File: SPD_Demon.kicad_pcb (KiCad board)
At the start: 2 copper layers, 146 x 21.1 mm, 3 parts, among them J1 Conn_02x84_Top_Bottom, U1 AT24CS02-SSHM, U2 AT24CS02-SSHM

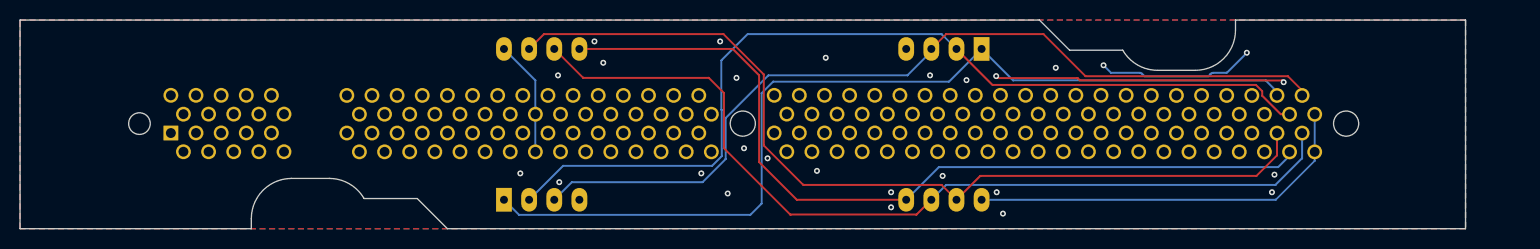
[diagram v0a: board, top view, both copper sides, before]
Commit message: Updated layout with single notch
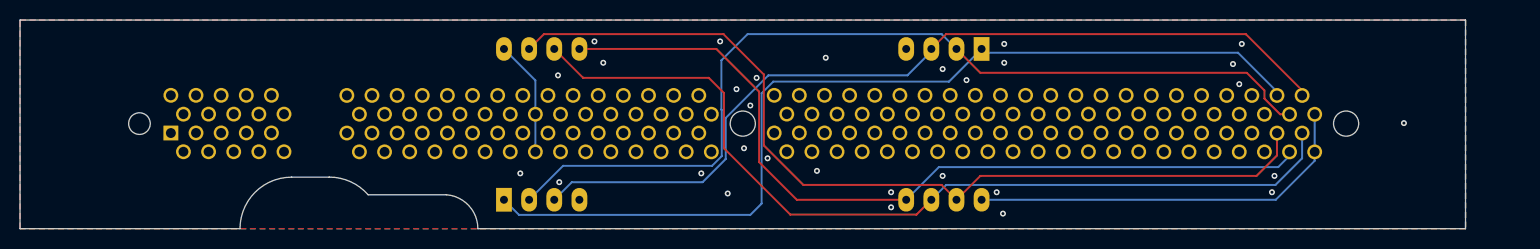
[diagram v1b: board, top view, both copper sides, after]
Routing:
- net GND: track 45.2 -> 0.00 mm, vias 27 -> 30
- net /SDA: track 85.4 -> 84.5 mm
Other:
- outline, holes or cut-outs redrawn

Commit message: v1 with silkscreen + gerbers
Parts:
- added G***: LOGO, SPD_Demon:OSHW, F.Cu at (166.0, 41.9)
- added G***: LOGO, SPD_Demon:JC, B.Cu at (31.0, 42.0)
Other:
- board text added: "SPD Demon"
- board text added: "for 168-pin RAM"
- board text added: "github.com/totallyobsolete/SPD_Demon"
- board text added: "v1.0"
